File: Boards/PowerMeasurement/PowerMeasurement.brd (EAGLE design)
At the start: 26 x 24.1 mm, 10 parts

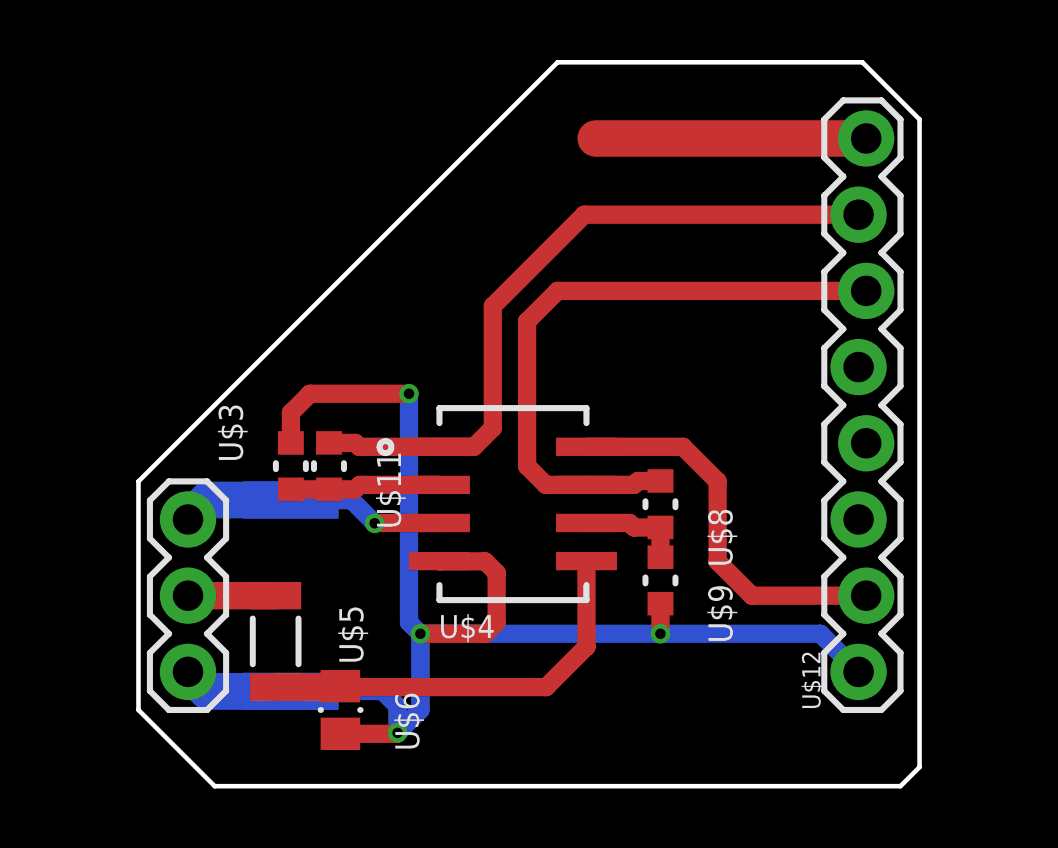
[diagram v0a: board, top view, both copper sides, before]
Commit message: Just added a small lip for mechanical relief on the connectors
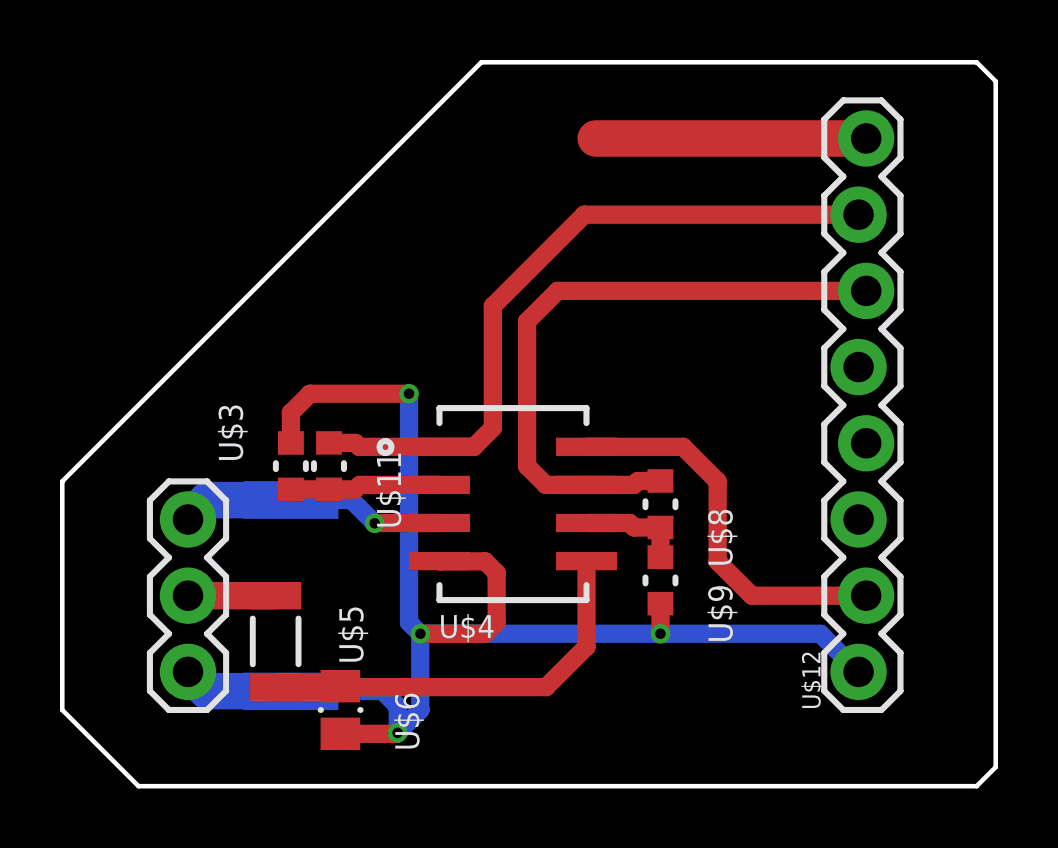
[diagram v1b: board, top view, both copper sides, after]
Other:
- board size 26 x 24.1 mm -> 31.1 x 24.1 mm
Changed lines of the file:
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@@
 <setting verticaltext="up"/>
 </settings>
-<grid distance="5" unitdist="mil" unit="mil" style="lines" multiple="1" display="yes" altdistance="5" altunitdist="mil" altunit="mil"/>
+<grid distance="50" unitdist="mil" unit="mil" style="lines" multiple="1" display="yes" altdistance="5" altunitdist="mil" altunit="mil"/>
 <layers>
 <layer number="1" name="Top" color="4" fill="1" visible="yes" active="yes"/>
@@
 <board>
 <plain>
-<wire x1="1.27" y1="2.54" x2="1.27" y2="10.16" width="0.1524" layer="20"/>
-<wire x1="1.27" y1="10.16" x2="15.24" y2="24.13" width="0.1524" layer="20"/>
-<wire x1="15.24" y1="24.13" x2="25.4" y2="24.13" width="0.1524" layer="20"/>
-<wire x1="25.4" y1="24.13" x2="27.305" y2="22.225" width="0.1524" layer="20"/>
-<wire x1="27.305" y1="22.225" x2="27.305" y2="0.635" width="0.1524" layer="20"/>
-<wire x1="27.305" y1="0.635" x2="26.67" y2="0" width="0.1524" layer="20"/>
-<wire x1="26.67" y1="0" x2="3.81" y2="0" width="0.1524" layer="20"/>
-<wire x1="3.81" y1="0" x2="1.27" y2="2.54" width="0.1524" layer="20"/>
+<wire x1="-1.27" y1="2.54" x2="-1.27" y2="10.16" width="0.1524" layer="20"/>
+<wire x1="-1.27" y1="10.16" x2="12.7" y2="24.13" width="0.1524" layer="20"/>
+<wire x1="12.7" y1="24.13" x2="29.21" y2="24.13" width="0.1524" layer="20"/>
+<wire x1="29.21" y1="24.13" x2="29.845" y2="23.495" width="0.1524" layer="20"/>
+<wire x1="29.845" y1="23.495" x2="29.845" y2="0.635" width="0.1524" layer="20"/>
+<wire x1="29.845" y1="0.635" x2="29.21" y2="0" width="0.1524" layer="20"/>
+<wire x1="29.21" y1="0" x2="1.27" y2="0" width="0.1524" layer="20"/>
+<wire x1="1.27" y1="0" x2="-1.27" y2="2.54" width="0.1524" layer="20"/>
 <polygon width="0.0508" layer="29">
 <vertex x="16.637" y="22.225"/>
